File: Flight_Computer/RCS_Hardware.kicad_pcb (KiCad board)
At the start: 2 copper layers, 60 x 52 mm, 55 parts, among them J2 TYPE-C-31-M-12, J4 5V, J8 Conn_01x05_Male, U1 STM32F401CCU6, U2 AMS1117-3.3, U4 BNO055, U5 W25Q32JVSS, U6 MPU-6050, Y1 16MHz, Y2 32.768Mhz

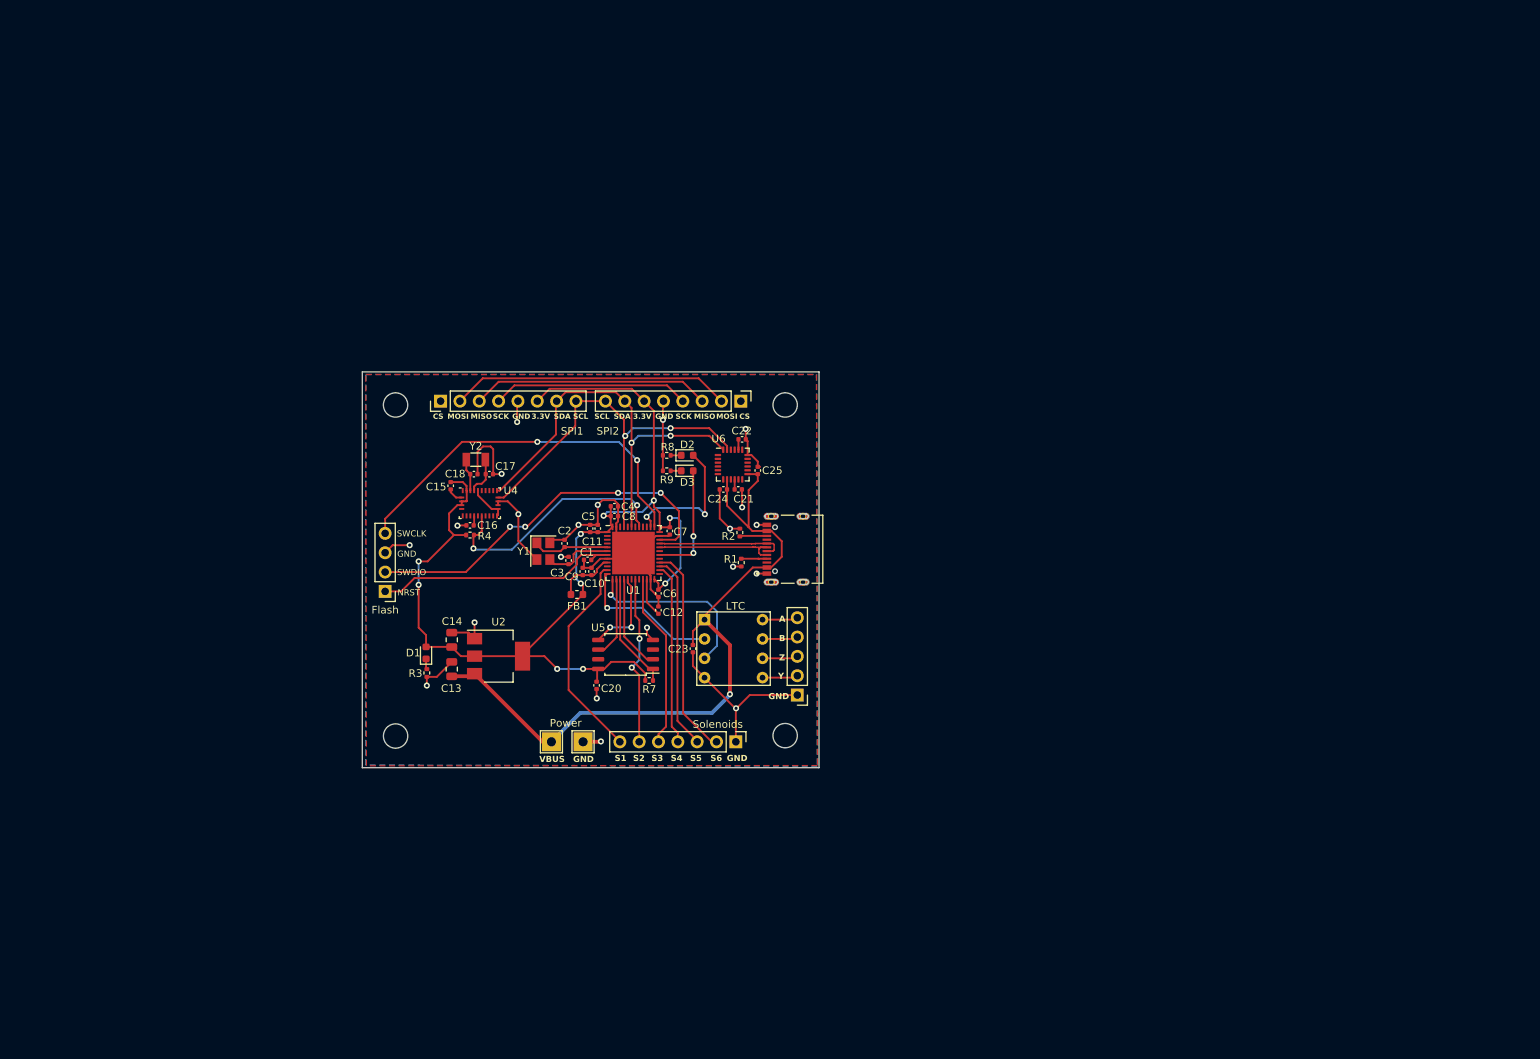
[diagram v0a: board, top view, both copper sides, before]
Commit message: placed components on gyroscope PCB
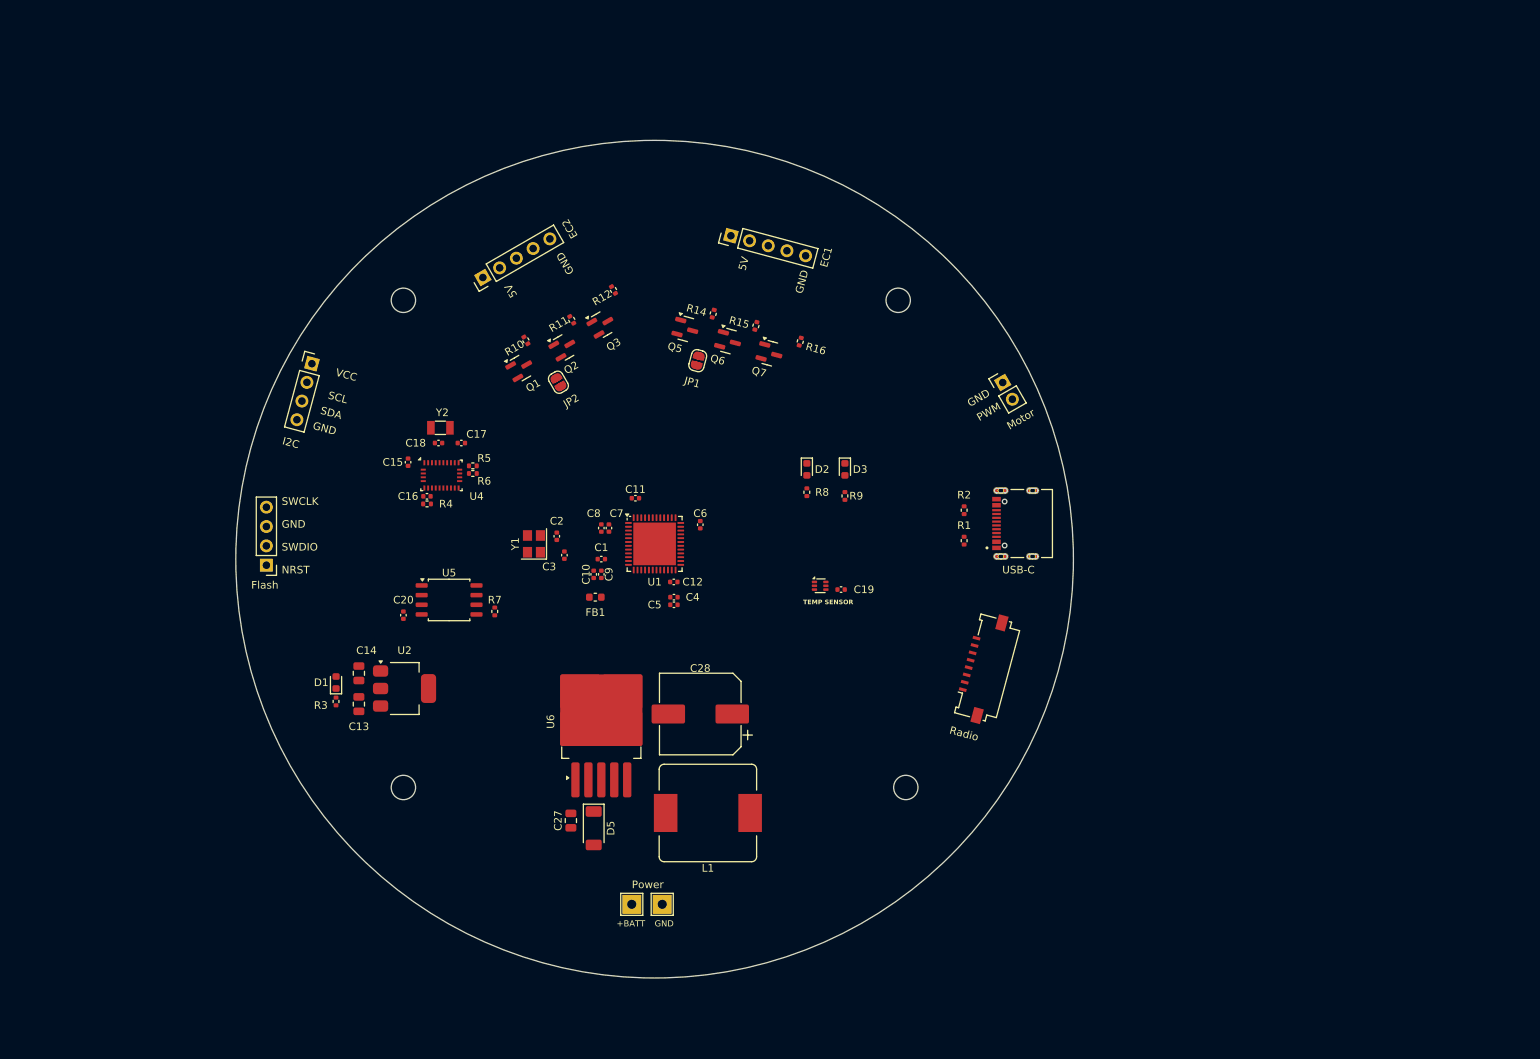
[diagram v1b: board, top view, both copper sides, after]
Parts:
- removed C21, C24: 0.1uF, Capacitor_SMD:C_0402_1005Metric
- removed C22: 2.2nF, Capacitor_SMD:C_0402_1005Metric
- removed C23: 100nF, Capacitor_SMD:C_0402_1005Metric
- removed C25: 10nF, Capacitor_SMD:C_0402_1005Metric
- removed Flash: SWD, Connector_PinHeader_2.54mm:PinHeader_1x04_P2.54mm_Vertical
- removed J8: Conn_01x05_Male, Connector_PinHeader_2.54mm:PinHeader_1x05_P2.54mm_Vertical
- removed LTC: LTC1690N8, LTC1690N8:LTC1690N8
- removed Power: GND, TestPoint:TestPoint_THTPad_2.5x2.5mm_Drill1.2mm
- removed SPI1, SPI2: SPI, Connector_PinHeader_2.54mm:PinHeader_1x08_P2.54mm_Vertical
- removed Solenoids: Solenoids, Connector_PinHeader_2.54mm:PinHeader_1x07_P2.54mm_Vertical
- added C19: 0.1uF, Capacitor_SMD:C_0402_1005Metric, F.Cu at (164.5, 104.0)
- added C27: 150uF, Capacitor_SMD:C_0805_2012Metric, F.Cu at (129.0, 134.3)
- added C28: 680uF, Capacitor_SMD:CP_Elec_10x10.5, F.Cu at (146.0, 120.3)
- added D5: PMEG4050EP, Diode_SMD:D_SOD-128, F.Cu at (132.0, 135.3)
- added J1: SWD, Connector_PinHeader_2.54mm:PinHeader_1x04_P2.54mm_Vertical, F.Cu at (89.0, 100.8)
- added J10: Motor, Connector_PinHeader_2.54mm:PinHeader_1x02_P2.54mm_Vertical, F.Cu at (185.7, 76.8)
- added J3: I2C, Connector_PinHeader_2.54mm:PinHeader_1x04_P2.54mm_Vertical, F.Cu at (95.0, 74.3)
- added J5: GND, TestPoint:TestPoint_THTPad_2.5x2.5mm_Drill1.2mm, F.Cu at (141.0, 145.3)
- added J6: AMT102, Connector_PinHeader_2.54mm:PinHeader_1x05_P2.54mm_Vertical, F.Cu at (150.0, 57.5)
- added J7: FC_RF, Connector_FFC-FPC:Molex_200528-0080_1x08-1MP_P1.00mm_Horizontal, F.Cu at (182.3, 114.0)
- added J9: AMT102, Connector_PinHeader_2.54mm:PinHeader_1x05_P2.54mm_Vertical, F.Cu at (117.4, 63.0)
- added JP1: SolderJumper_2_Open, Jumper:SolderJumper-2_P1.3mm_Open_RoundedPad1.0x1.5mm, F.Cu at (145.7, 73.9)
- added JP2: SolderJumper_2_Open, Jumper:SolderJumper-2_P1.3mm_Open_RoundedPad1.0x1.5mm, F.Cu at (127.4, 76.8)
- added L1: 100uH, Inductor_SMD:L_TaiTech_TMPC1265_13.5x12.5mm, F.Cu at (147.0, 133.3)
- added Q1: 2N7002, Package_TO_SOT_SMD:SOT-23, F.Cu at (122.4, 74.9)
- added Q2: 2N7002, Package_TO_SOT_SMD:SOT-23, F.Cu at (128.0, 72.2)
- added Q3: 2N7002, Package_TO_SOT_SMD:SOT-23, F.Cu at (133.0, 69.2)
- added Q5: 2N7002, Package_TO_SOT_SMD:SOT-23, F.Cu at (144.1, 69.8)
- added Q6: 2N7002, Package_TO_SOT_SMD:SOT-23, F.Cu at (149.7, 71.4)
- added Q7: 2N7002, Package_TO_SOT_SMD:SOT-23, F.Cu at (155.1, 73.0)
- added R10: 1k, Resistor_SMD:R_0402_1005Metric, F.Cu at (123.1, 71.3)
- added R11: 1k, Resistor_SMD:R_0402_1005Metric, F.Cu at (129.1, 68.6)
- added R12: 1k, Resistor_SMD:R_0402_1005Metric, F.Cu at (134.6, 64.6)
- added R14: 1k, Resistor_SMD:R_0402_1005Metric, F.Cu at (147.7, 67.8)
- added R15: 1k, Resistor_SMD:R_0402_1005Metric, F.Cu at (153.3, 69.4)
- added R16: 1k, Resistor_SMD:R_0402_1005Metric, F.Cu at (159.1, 71.4)
- added R5: 10k, Resistor_SMD:R_0402_1005Metric, F.Cu at (116.1, 87.8)
- added R6: 10k, Resistor_SMD:R_0402_1005Metric, F.Cu at (116.1, 88.8)
- added U3: TMP102xxDRL, Package_TO_SOT_SMD:SOT-563, F.Cu at (161.8, 103.5)
- U6: value MPU-6050 -> LM2576S-5; footprint Sensor_Motion:InvenSense_QFN-24_4x4mm_P0.5mm -> Package_TO_SOT_SMD:TO-263-5_TabPin3
- moved H3 67.4 mm to (173.0, 130.0)
- moved H4 50.6 mm to (107.0, 130.0)
- moved U6 37.9 mm to (133.0, 121.3), turned to 90 degrees
- moved J2 30.4 mm to (189.7, 95.3)
- moved R2 29.6 mm to (180.7, 93.6)
- moved R1 29.4 mm to (180.7, 97.6)
- moved C20 27.0 mm to (107.0, 107.4), turned to 90 degrees
- moved U5 24.3 mm to (113.0, 105.4), turned to 0 degrees
- moved J4 23.8 mm to (137.0, 145.3), turned to 90 degrees
- moved R9 23.6 mm to (165.0, 91.7), turned to -90 degrees
- moved R7 22.2 mm to (119.0, 106.9), turned to 90 degrees
- moved D3 20.7 mm to (165.0, 88.2), turned to -90 degrees
- moved H2 20.2 mm to (172.0, 66.0)
- moved R8 19.0 mm to (160.0, 91.2), turned to -90 degrees
- moved D2 15.8 mm to (160.0, 88.2), turned to -90 degrees
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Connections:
- C13 pad 1: VBUS -> +5V
- J2 pad A4/B9: VBUS -> +5V
- J2 pad B4/A9: VBUS -> +5V
- J4 pad 1: VBUS -> +BATT
- U1 pad 20: unconnected-(U1-PB2-Pad20) -> /I2
- U1 pad 21: /S3 -> unconnected-(U1-PB10-Pad21)
- U1 pad 29: unconnected-(U1-PA8-Pad29) -> /SCL
- U1 pad 39: unconnected-(U1-PB3-Pad39) -> /I1
- U1 pad 40: unconnected-(U1-PB4-Pad40) -> /SDA
- U1 pad 42: unconnected-(U1-PB6-Pad42) -> /E1B
- U1 pad 43: /SDA -> /E2B
- U1 pad 45: /SCL -> /E1A
- U1 pad 46: unconnected-(U1-PB9-Pad46) -> /E2A
- U2 pad 3: VBUS -> +5V
- U4 pad 5: unconnected-(U4-PS1-Pad5) -> GND
- U4 pad 6: unconnected-(U4-PS0-Pad6) -> GND
- U5 pad 1: /SCLK -> /CS_FLASH
- U5 pad 6: /CS_FLASH -> /SCLK
- U6 pad 1: /CLKIN -> +BATT
- U6 pad 2: unconnected-(U6-NC-Pad2) -> Net-(D5-K)
- U6 pad 3: unconnected-(U6-NC-Pad3) -> GND
- U6 pad 4: unconnected-(U6-NC-Pad4) -> +5V
- U6 pad 5: unconnected-(U6-NC-Pad5) -> GND
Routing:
- net +3.3V: track 148.9 -> 0.00 mm, vias 10 -> 0
- net GND: track 144.3 -> 0.00 mm, vias 21 -> 0
- net VBUS: track 96.1 -> 0.00 mm, vias 1 -> 0
- net /SDA: track 55.4 -> 0.00 mm, vias 2 -> 0
- net /SCL: track 54.0 -> 0.00 mm, vias 2 -> 0
- net /SWDIO: track 50.4 -> 0.00 mm, vias 4 -> 0
- net /SWCLK: track 49.9 -> 0.00 mm, vias 2 -> 0
- net /MOSI2: track 36.8 -> 0.00 mm
- net /NRST: track 34.0 -> 0.00 mm
- net /BNO_NRST: track 32.7 -> 0.00 mm, vias 2 -> 0
- net /MISO2: track 31.4 -> 0.00 mm
- net /S6: track 27.9 -> 0.00 mm
- net /S1: track 27.7 -> 0.00 mm
- net /SCK: track 25.9 -> 0.00 mm
- net /S5: track 25.6 -> 0.00 mm
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- removed copper zone on B.Cu, net GND
- removed copper zone on F.Cu, net GND
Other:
- board size 60 x 52 mm -> 110 x 110 mm
- board text added: "+BATT"
- board text added: "5V"
- board text added: "EC1"
- board text added: "EC2"
- board text added: "Flash"
- board text added: "I2C"
- board text added: "Motor"
- board text added: "PWM"
- board text added: "Power"
- board text added: "Radio"
- board text added: "TEMP SENSOR"
- board text added: "USB-C"
- board text added: "VCC"
- board text removed: "3.3V"
- board text removed: "A"
- board text removed: "B"
- board text removed: "C10"
- board text removed: "CS"
- board text removed: "MISO"
- board text removed: "MOSI"
- board text removed: "Reaction Control System Society For Advanced Rocket Propulsion"
- board text removed: "S1"
- board text removed: "S2"
- board text removed: "S3"
- board text removed: "S4"
- board text removed: "S5"
- board text removed: "S6"
- board text removed: "SCK"
- board text removed: "SPI1"
- board text removed: "SPI2"
- board text removed: "VBUS"
- board text removed: "Y"
- board text removed: "Z"

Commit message: moved usb-c connector position
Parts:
- moved J2 4.13 mm to (193.0, 97.8)
- moved R1 4.13 mm to (184.0, 100.0)
- moved R2 4.13 mm to (184.0, 96.0)
